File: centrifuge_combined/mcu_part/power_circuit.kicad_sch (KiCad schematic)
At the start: 64 parts

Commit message: Almost finished releasable version
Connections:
- net VIN: now reaches C507.1, C508.1, C509.1, C510.1, C511.1, C512.1, C513.1, C523.1, C524.1, C525.1, C526.1, C527.1, C528.1, J509.1 (VBUS), Q501.3 (S), U503.1 (VIN1), U503.16 (VIN2), U503.5 (EN1), U504.1 (VIN1), U504.16 (VIN2), U505.1 (VIN1), U505.16 (VIN2)
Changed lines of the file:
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@@
   (junction (at 200.025 121.92) (diameter 0) (color 0 0 0 0)
+  )
+  (junction (at 74.295 44.704) (diameter 0) (color 0 0 0 0)
   )
   (junction (at 143.51 158.75) (diameter 0) (color 0 0 0 0)
@@
     (stroke (width 0) (type default) (color 0 0 0 0))
   )
+  (wire (pts (xy 69.6976 44.704) (xy 74.295 44.704))
+    (stroke (width 0) (type default) (color 0 0 0 0))
+  )
   (wire (pts (xy 143.51 158.75) (xy 151.13 158.75))
     (stroke (width 0) (type default) (color 0 0 0 0))
@@
     (stroke (width 0) (type default) (color 0 0 0 0))
   )
-  (wire (pts (xy 74.295 16.51) (xy 74.295 64.135))
+  (wire (pts (xy 74.295 16.51) (xy 74.295 44.704))
     (stroke (width 0) (type default) (color 0 0 0 0))
   )
@@
   )
   (wire (pts (xy 227.965 81.28) (xy 227.965 106.68))
+    (stroke (width 0) (type default) (color 0 0 0 0))
+  )
+  (wire (pts (xy 74.295 44.704) (xy 74.295 64.135))
     (stroke (width 0) (type default) (color 0 0 0 0))
   )
@@
     (effects (font (size 1.27 1.27)) (justify left bottom))
   )
+  (label "VIN" (at 69.6976 44.704 180)
+    (effects (font (size 1.27 1.27)) (justify right bottom))
+  )
   (hierarchical_label "1V8" (shape output) (at 271.78 30.48 0)

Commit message: Board appears ok
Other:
- title: Power supply -> VGA Centrifuge
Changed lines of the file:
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@@
   (paper "A4")
   (title_block
-    (title "Power supply")
+    (title "VGA Centrifuge")
+    (date "2022-10-03")
+    (rev "R2")
   )
   (junction (at 151.13 158.75) (diameter 0) (color 0 0 0 0)

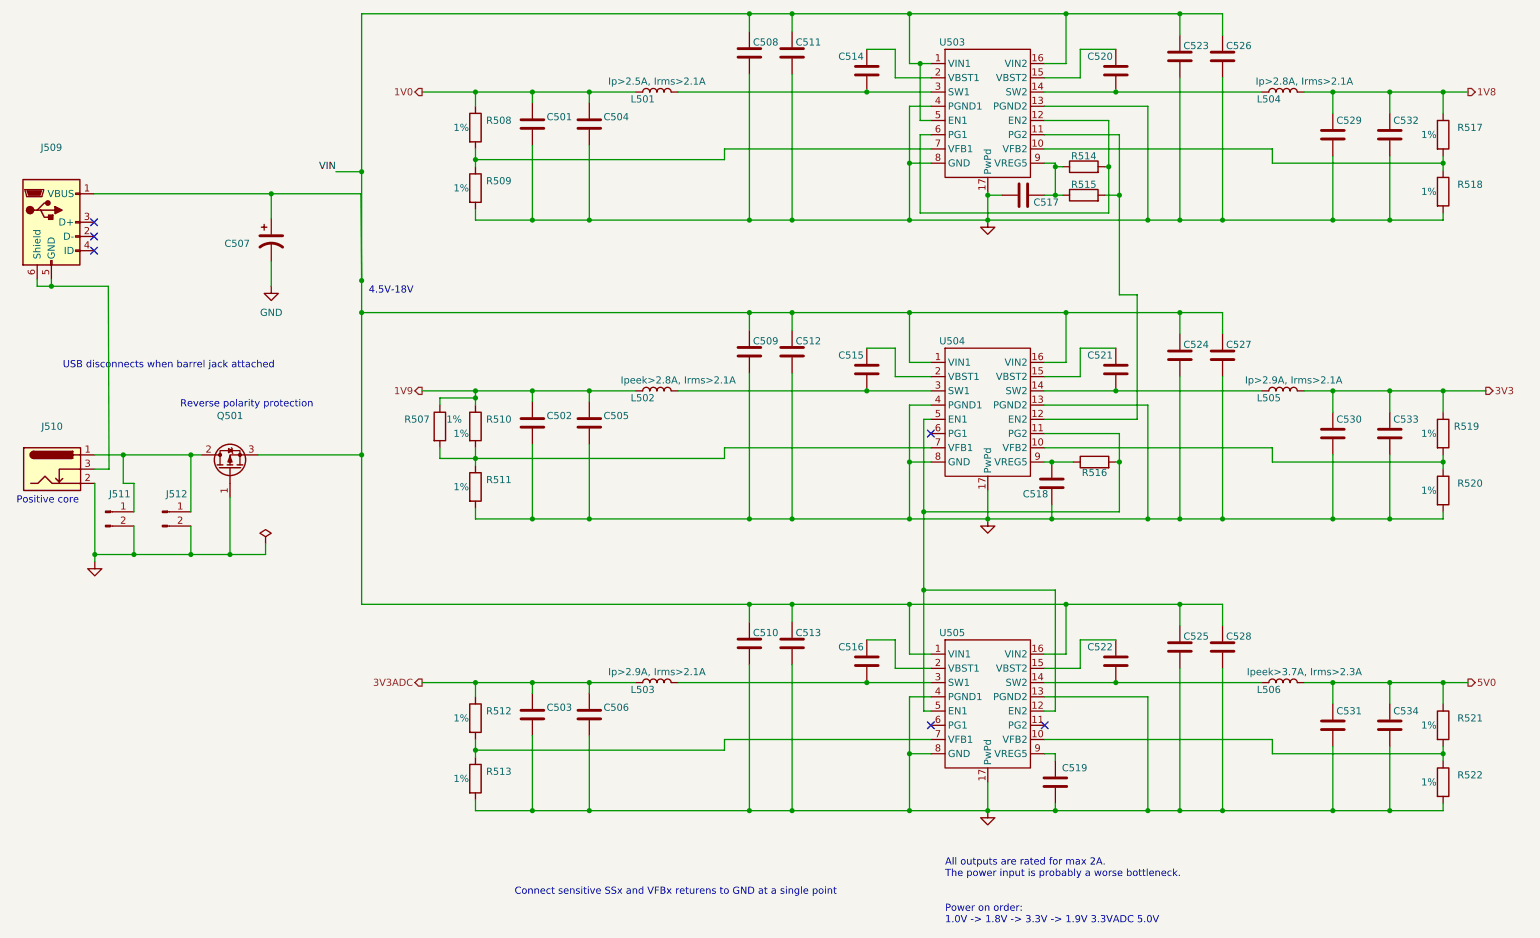
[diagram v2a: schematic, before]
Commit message: fixed keypad hole sizes, and submitted
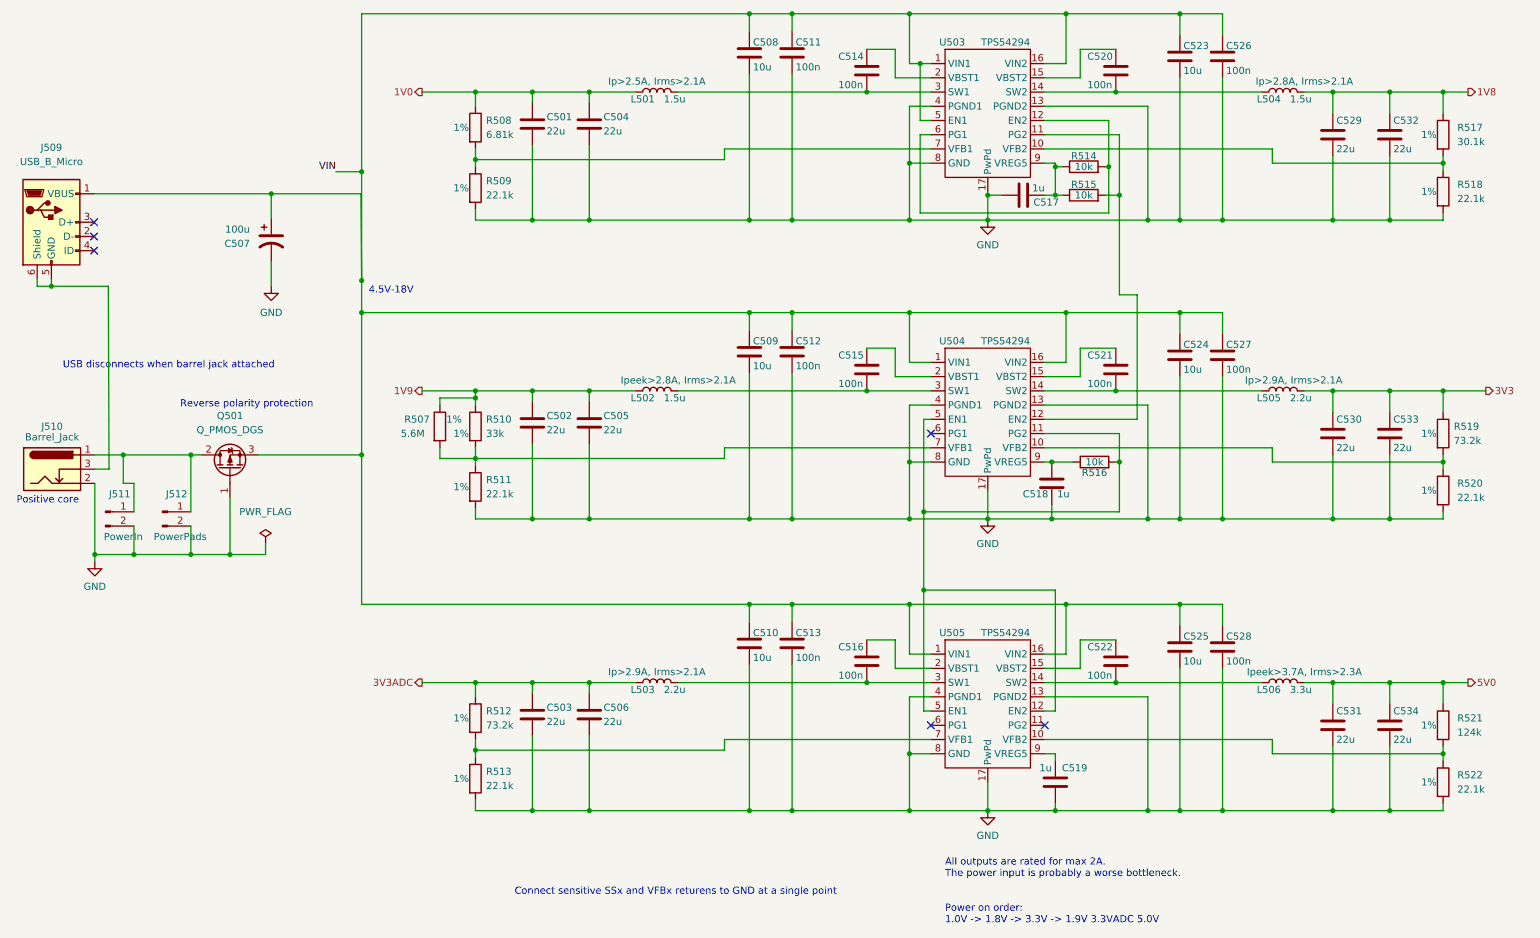
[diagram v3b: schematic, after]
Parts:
- C501, C502, C503, C504, C505, C506, C529, C530, C531, C532, C533, C534: value (none) -> 22u
- C507: value (none) -> 100u
- C508, C509, C510, C523, C524, C525: value (none) -> 10u
- C511, C512, C513, C514, C515, C516, C520, C521, C522, C526, C527, C528: value (none) -> 100n
- C517, C518, C519: value (none) -> 1u
- J509: value (none) -> USB_B_Micro
- J510: value (none) -> Barrel_Jack
- J511: value (none) -> PowerIn
- J512: value (none) -> PowerPads
- L501, L502, L504: value (none) -> 1.5u
- L503, L505: value (none) -> 2.2u
- L506: value (none) -> 3.3u
- Q501: value (none) -> Q_PMOS_DGS
- R507: value (none) -> 5.6M
- R508: value (none) -> 6.81k
- R509, R511, R513, R518, R520, R522: value (none) -> 22.1k
- R510: value (none) -> 33k
- R512, R519: value (none) -> 73.2k
- R514, R515, R516: value (none) -> 10k
- R517: value (none) -> 30.1k
- R521: value (none) -> 124k
- U503, U504, U505: value (none) -> TPS54294

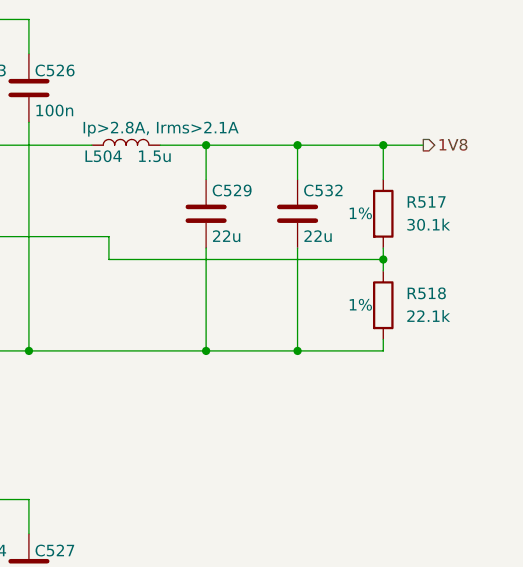
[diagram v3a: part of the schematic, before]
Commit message: create new PSU routing for all 6 voltages
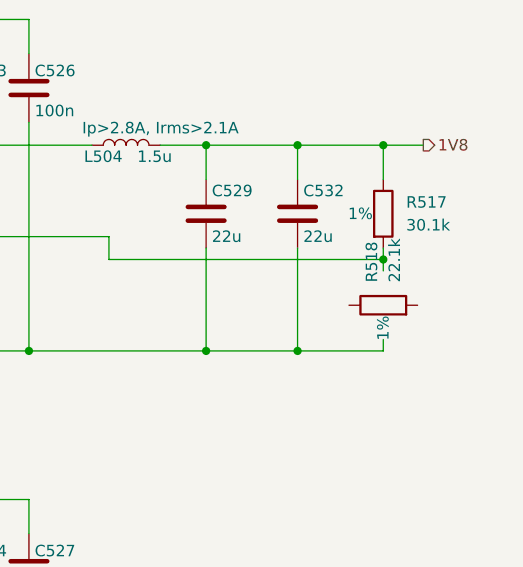
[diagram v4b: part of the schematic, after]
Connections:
- net GND: no longer R518.2
- net at R517.2, U503.10 (VFB2): no longer R518.1
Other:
- moved on the sheet: R518
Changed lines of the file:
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@@
     (pin "2")
   )
-  (symbol (lib_id "Device:R") (at 267.335 48.26 0) (unit 1)
+  (symbol (lib_id "Device:R") (at 267.335 48.26 90) (unit 1)
     (in_bom yes) (on_board yes)
-    (property "Reference" "R518" (id 0) (at 269.875 46.9899 0)
+    (property "Reference" "R518" (id 0) (at 266.0649 45.72 0)
       (effects (font (size 1.27 1.27)) (justify left))
     )
-    (property "Value" "22.1k" (id 1) (at 269.875 49.5299 0)
+    (property "Value" "22.1k" (id 1) (at 268.6049 45.72 0)
       (effects (font (size 1.27 1.27)) (justify left))
     )
-    (property "Footprint" "" (id 2) (at 265.557 48.26 90)
+    (property "Footprint" "" (id 2) (at 267.335 50.038 90)
       (effects (font (size 1.27 1.27)) hide)
     )
@@
       (effects (font (size 1.27 1.27)) hide)
     )
-    (property "Tolerance" "1%" (id 4) (at 264.795 48.26 0))
+    (property "Tolerance" "1%" (id 4) (at 267.335 50.8 0))
     (property "Purchase" "https://www.digikey.no/no/products/detail/stackpole-electronics-inc/RNCP0805FTD22K1/2240273" (id 5) (at 267.335 48.26 0)
       (effects (font (size 1.27 1.27)) hide)

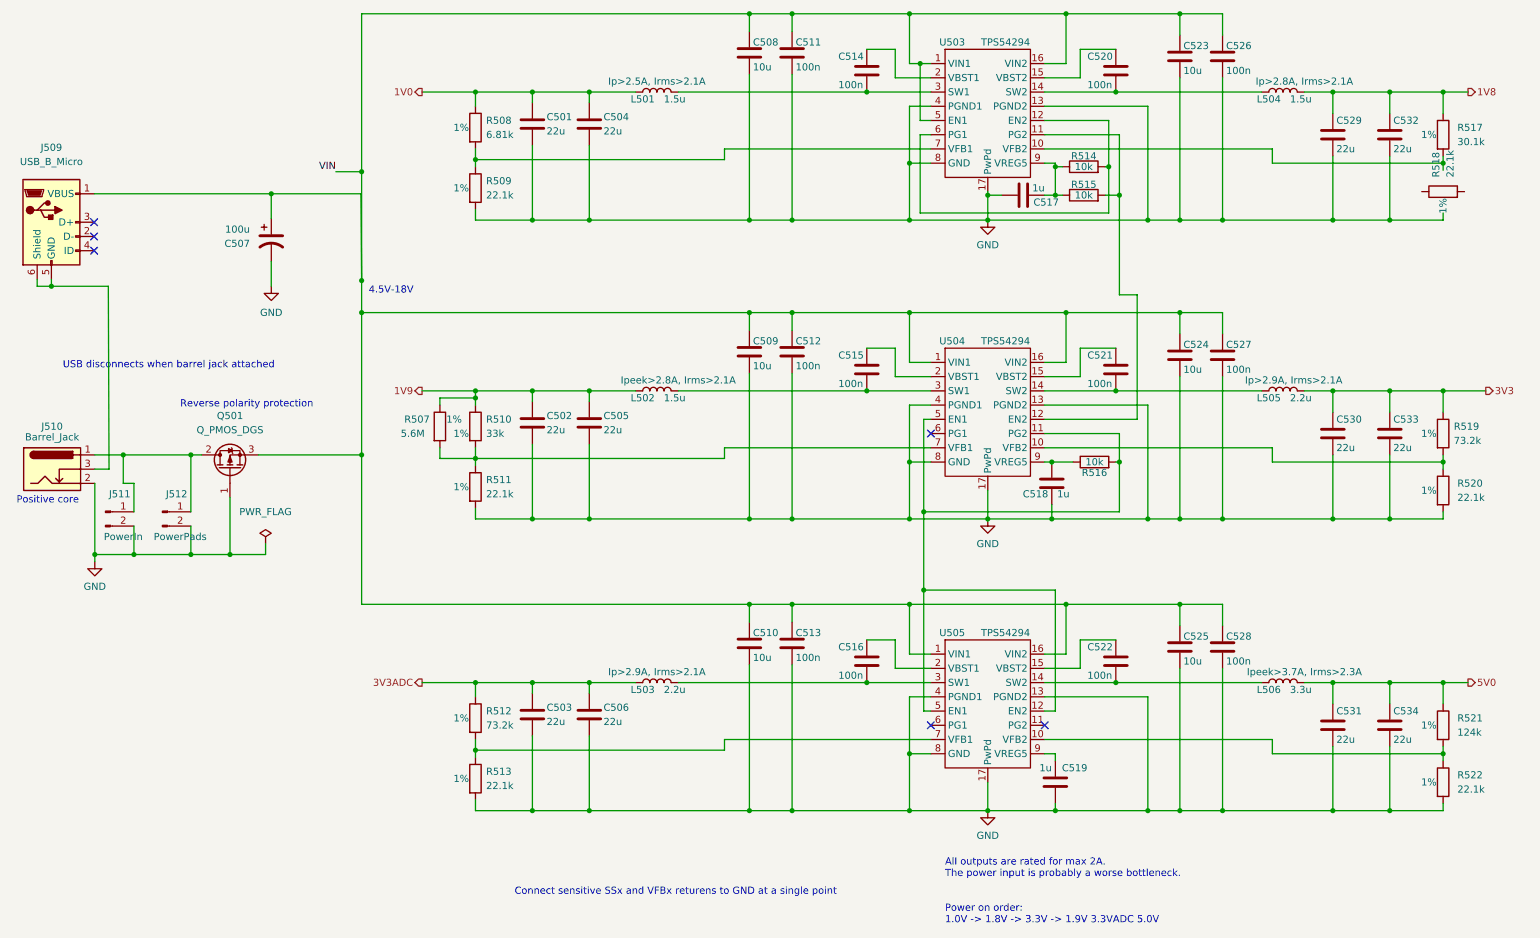
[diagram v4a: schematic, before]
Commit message: Fixed missing footprints, added decoupling capacitors, adjusted board edges
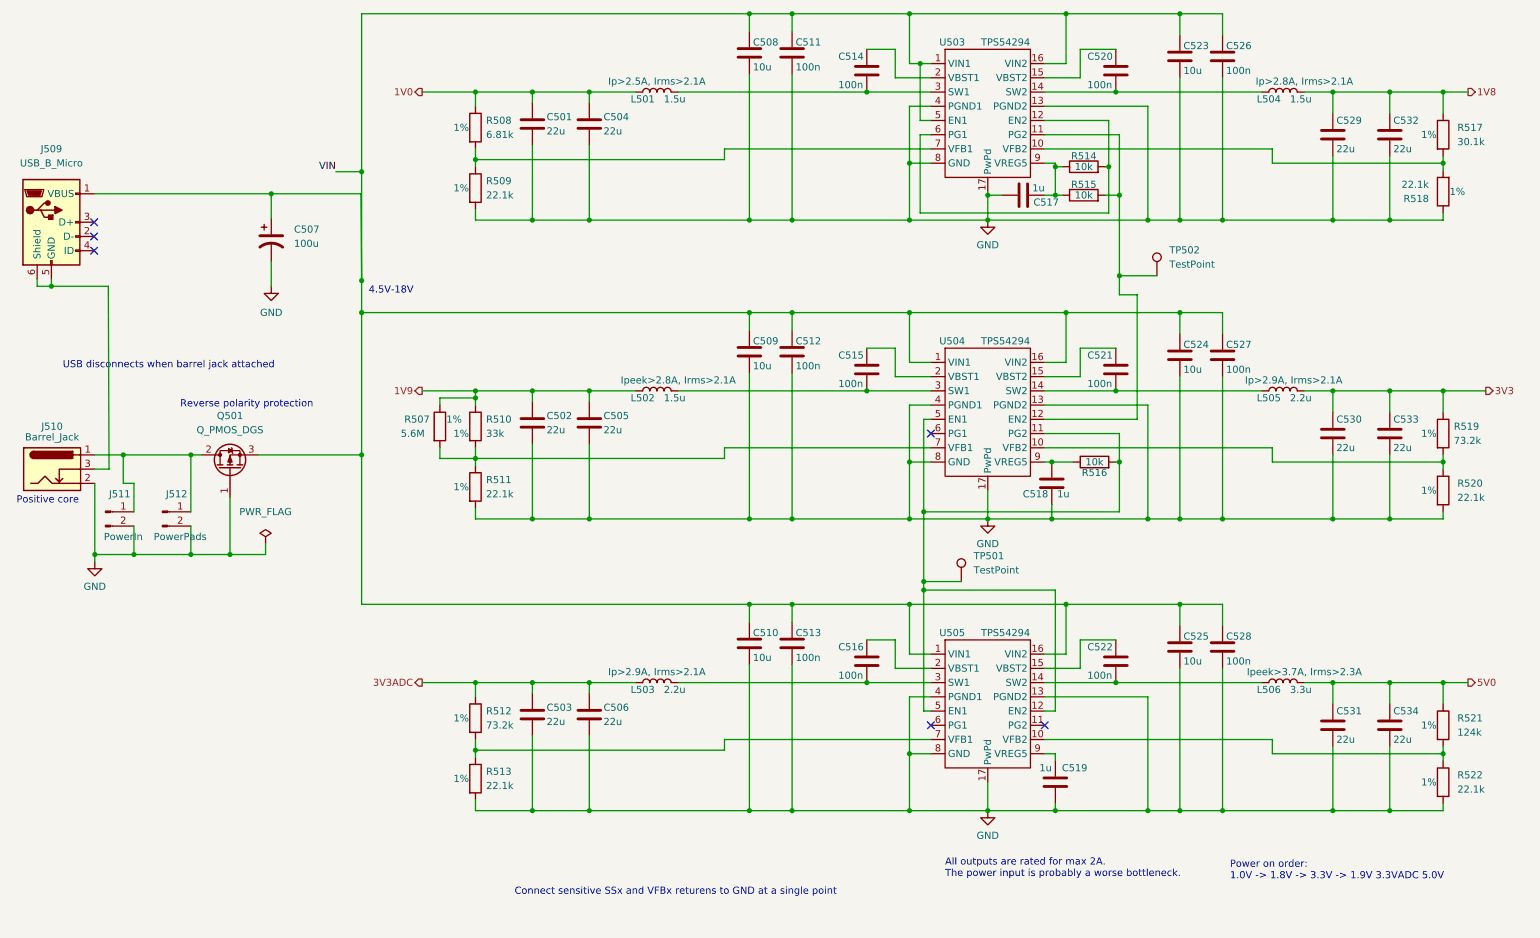
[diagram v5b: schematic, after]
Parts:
- added TP501, TP502: TestPoint, TestPoint:TestPoint_Keystone_5015_Micro-Minature, symbol Connector:TestPoint
- C501, C502, C503, C504, C505, C506, C508, C509, C510, C511, C512, C513, C514, C515, C516, C520, C521, C522, C523, C524, C525, C526, C527, C528, C529, C530, C531, C532, C533, C534: footprint (none) -> Capacitor_SMD:C_1206_3216Metric_Pad1.33x1.80mm_HandSolder
- C507: footprint (none) -> Capacitor_THT:CP_Radial_D10.0mm_P5.00mm
- C517, C518, C519: footprint (none) -> Capacitor_SMD:C_0805_2012Metric_Pad1.18x1.45mm_HandSolder
- J509: footprint (none) -> Connector_USB:USB_Micro-B_Molex-105017-0001
- J510: footprint (none) -> Connector_BarrelJack:BarrelJack_CUI_PJ-102AH_Horizontal
- J511: footprint (none) -> Connector_PinHeader_2.54mm:PinHeader_1x02_P2.54mm_Vertical
- J512: footprint (none) -> centrifuge_mcu:PowerPads
- L501, L502, L504: footprint (none) -> centrifuge_mcu:L_Sumida_CR75
- L503, L505: footprint (none) -> Inductor_SMD:L_Vishay_IHLP-2020
- L506: footprint (none) -> centrifuge_mcu:L_TDK_7065
- Q501: footprint (none) -> Package_TO_SOT_THT:TO-220-3_Vertical
- R507, R508, R509, R510, R511, R512, R513, R514, R515, R516, R517, R518, R519, R520, R521, R522: footprint (none) -> Resistor_SMD:R_0805_2012Metric_Pad1.20x1.40mm_HandSolder
- U503, U504, U505: footprint (none) -> centrifuge_mcu:TSSOP-16-1EP_4.4x5mm_P0.65mm_EP3x3mm_ThermalVias_EXTRA
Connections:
- net GND: now also R518.1
- net at R516.2, U504.11 (PG2), U504.5 (EN1)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: now also TP501.1
- net at R515.2, U503.11 (PG2), U504.12 (EN2): now also TP502.1
- net at R518.2: now also R517.2, U503.10 (VFB2)
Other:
- moved on the sheet: R518

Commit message: remove digikey links to products that we already buy from mouser, add mouser link instead
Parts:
- C517, C518, C519: Order Page (none) -> https://no.mouser.com/ProductDetail/Walsin/0805X105K100CT?q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; Purchase https://www.digikey.no/no/products/detail/kemet/C0805C105J4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 -> (none)
- R514, R515, R516: Order Page (none) -> https://no.mouser.com/ProductDetail/YAGEO/RC0805FR-1310KL?q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; Purchase https://www.digikey.no/no/products/detail/yageo/AC0805FR-07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 -> (none)
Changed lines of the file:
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@@
       (effects (font (size 1.27 1.27)) hide)
     )
-    (property "Purchase" "https://www.digikey.no/no/products/detail/yageo/AC0805FR-07100KL/5896520" (id 4) (at 203.2 43.815 0)
+    (property "Purchase" "" (id 4) (at 203.2 43.815 0)
+      (effects (font (size 1.27 1.27)) hide)
+    )
+    (property "Order Page" "https://no.mouser.com/ProductDetail/YAGEO/RC0805FR-1310KL?qs=sGAEpiMZZMtlubZbdhIBIHucEnbnlIRRGobQQ23C9vc%3D" (id 5) (at 203.2 43.815 0)
       (effects (font (size 1.27 1.27)) hide)
     )
@@
       (effects (font (size 1.27 1.27)) hide)
     )
-    (property "Purchase" "https://www.digikey.no/no/products/detail/kemet/C0805C105J4REC7800/8643700" (id 4) (at 197.485 100.33 0)
+    (property "Purchase" "" (id 4) (at 197.485 100.33 0)
+      (effects (font (size 1.27 1.27)) hide)
+    )
+    (property "Order Page" "https://no.mouser.com/ProductDetail/Walsin/0805X105K100CT?qs=sGAEpiMZZMsh%252B1woXyUXj6GIMbU2VNPkBXHihtGsekQ%3D" (id 5) (at 197.485 100.33 0)
       (effects (font (size 1.27 1.27)) hide)
     )
@@
       (effects (font (size 1.27 1.27)) hide)
     )
-    (property "Purchase" "https://www.digikey.no/no/products/detail/kemet/C0805C105J4REC7800/8643700" (id 4) (at 198.12 153.67 0)
+    (property "Purchase" "" (id 4) (at 198.12 153.67 0)
+      (effects (font (size 1.27 1.27)) hide)
+    )
+    (property "Order Page" "https://no.mouser.com/ProductDetail/Walsin/0805X105K100CT?qs=sGAEpiMZZMsh%252B1woXyUXj6GIMbU2VNPkBXHihtGsekQ%3D" (id 5) (at 198.12 153.67 0)
       (effects (font (size 1.27 1.27)) hide)
     )
@@
       (effects (font (size 1.27 1.27)) hide)
     )
-    (property "Purchase" "https://www.digikey.no/no/products/detail/yageo/AC0805FR-0710KL/2827834" (id 4) (at 205.105 96.52 0)
+    (property "Purchase" "" (id 4) (at 205.105 96.52 0)
+      (effects (font (size 1.27 1.27)) hide)
+    )
+    (property "Order Page" "https://no.mouser.com/ProductDetail/YAGEO/RC0805FR-1310KL?qs=sGAEpiMZZMtlubZbdhIBIHucEnbnlIRRGobQQ23C9vc%3D" (id 5) (at 205.105 96.52 0)
       (effects (font (size 1.27 1.27)) hide)
     )
@@
       (effects (font (size 1.27 1.27)) hide)
     )
-    (property "Purchase" "https://www.digikey.no/no/products/detail/kemet/C0805C105J4REC7800/8643700" (id 4) (at 192.405 48.895 0)
+    (property "Purchase" "" (id 4) (at 192.405 48.895 0)
+      (effects (font (size 1.27 1.27)) hide)
+    )
+    (property "Order Page" "https://no.mouser.com/ProductDetail/Walsin/0805X105K100CT?qs=sGAEpiMZZMsh%252B1woXyUXj6GIMbU2VNPkBXHihtGsekQ%3D" (id 5) (at 192.405 48.895 0)
       (effects (font (size 1.27 1.27)) hide)
     )
@@
       (effects (font (size 1.27 1.27)) hide)
     )
-    (property "Purchase" "https://www.digikey.no/no/products/detail/yageo/AC0805FR-07100KL/5896520" (id 4) (at 203.2 48.895 0)
-      (effects (font (size 1.27 1.27)) hide)
-    )
+    (property "Purchase" "" (id 4) (at 203.2 48.895 0)
+      (effects (font (size 1.27 1.27)) hide)
+    )
+    (property "Order Page" "https://no.mouser.com/ProductDetail/YAGEO/RC0805FR-1310KL?qs=sGAEpiMZZMtlubZbdhIBIHucEnbnlIRRGobQQ23C9vc%3D" (id 5) (at 203.2 48.895 0)
+      (effects (font (size 1.27 1.27)) hide)
+    )
